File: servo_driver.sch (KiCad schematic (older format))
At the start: 16 parts

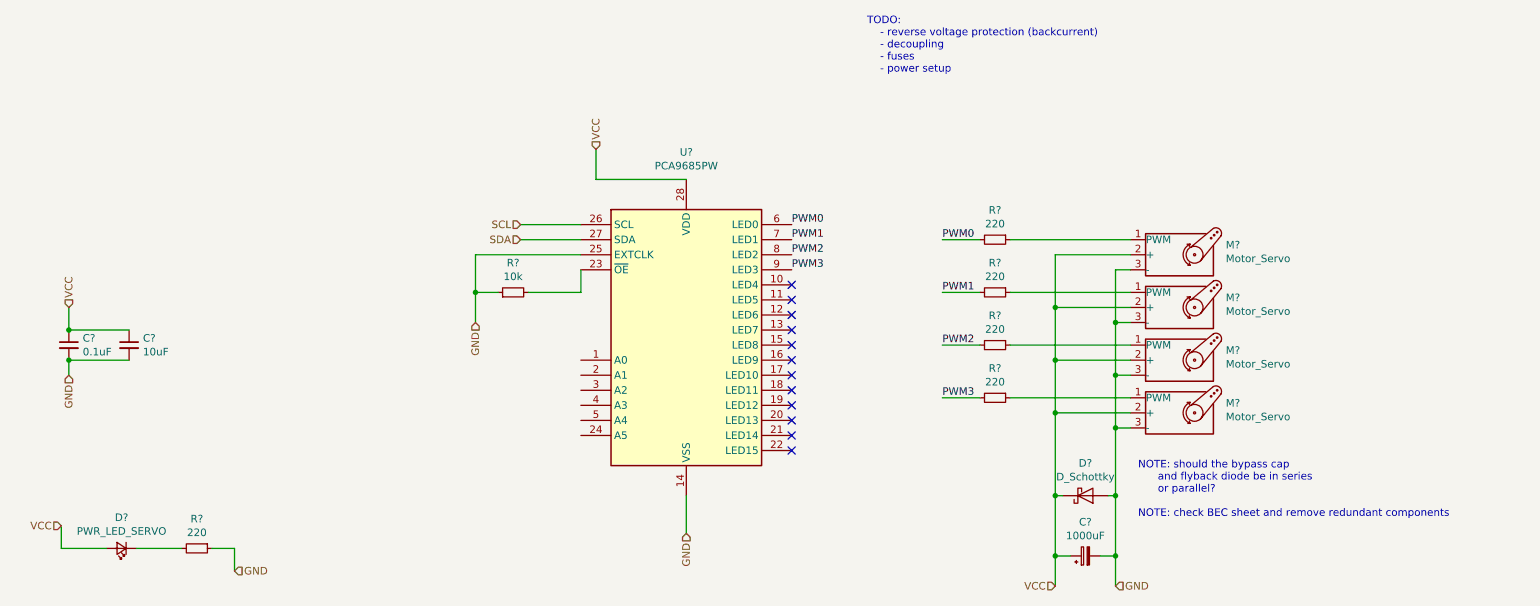
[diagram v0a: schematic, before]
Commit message: update reference ids, assign value to c8
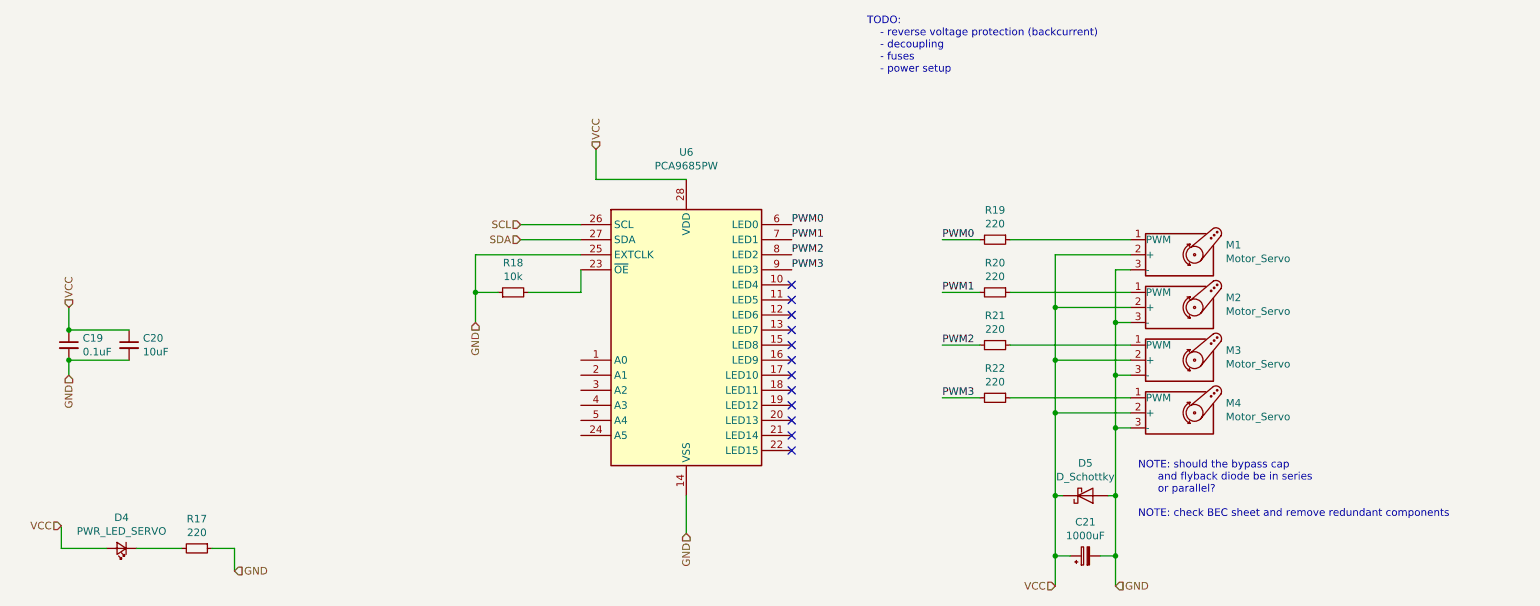
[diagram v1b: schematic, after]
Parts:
- gave numbers to parts that had none: 16
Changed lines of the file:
@@
 GND
 $Comp
-L Driver_LED:PCA9685PW U?
+L Driver_LED:PCA9685PW U6
 U 1 1 61AF04F5
 P 5800 3700
-F 0 "U?" H 5800 4881 50  0000 C CNN
+F 0 "U6" H 5800 4881 50  0000 C CNN
 F 1 "PCA9685PW" H 5800 4790 50  0000 C CNN
 F 2 "Package_SO:TSSOP-28_4.4x9.7mm_P0.65mm" H 5825 2725 50  0001 L CNN
@@
 $EndComp
 $Comp
-L Device:C_Small C?
+L Device:C_Small C20
 U 1 1 61AFE32D
 P 2100 3800
-F 0 "C?" H 2192 3846 50  0000 L CNN
+F 0 "C20" H 2192 3846 50  0000 L CNN
 F 1 "10uF" H 2192 3755 50  0000 L CNN
 F 2 "" H 2100 3800 50  0001 C CNN
@@
 $EndComp
 $Comp
-L Device:C_Small C?
+L Device:C_Small C19
 U 1 1 61AFE9E7
 P 1700 3800
-F 0 "C?" H 1792 3846 50  0000 L CNN
+F 0 "C19" H 1792 3846 50  0000 L CNN
 F 1 "0.1uF" H 1792 3755 50  0000 L CNN
 F 2 "" H 1700 3800 50  0001 C CNN
@@
 TODO:\n    - reverse voltage protection (backcurrent)\n    - decoupling\n    - fuses\n    - power setup\n
 $Comp
-L Device:R_Small R?
+L Device:R_Small R19
 U 1 1 61A44E55
 P 7850 3100
-F 0 "R?" V 7654 3100 50  0000 C CNN
+F 0 "R19" V 7654 3100 50  0000 C CNN
 F 1 "220" V 7745 3100 50  0000 C CNN
 F 2 "" H 7850 3100 50  0001 C CNN
@@
 $EndComp
 $Comp
-L Motor:Motor_Servo M?
+L Motor:Motor_Servo M1
 U 1 1 61AAC45D
 P 9050 3200
-F 0 "M?" H 9382 3265 50  0000 L CNN
+F 0 "M1" H 9382 3265 50  0000 L CNN
 F 1 "Motor_Servo" H 9382 3174 50  0000 L CNN
 F 2 "" H 9050 3010 50  0001 C CNN
@@
 $EndComp
 $Comp
-L Motor:Motor_Servo M?
+L Motor:Motor_Servo M2
 U 1 1 61AB6B78
 P 9050 3550
-F 0 "M?" H 9382 3615 50  0000 L CNN
+F 0 "M2" H 9382 3615 50  0000 L CNN
 F 1 "Motor_Servo" H 9382 3524 50  0000 L CNN
 F 2 "" H 9050 3360 50  0001 C CNN
@@
 $EndComp
 $Comp
-L Motor:Motor_Servo M?
+L Motor:Motor_Servo M3
 U 1 1 61AC1470
 P 9050 3900
-F 0 "M?" H 9382 3965 50  0000 L CNN
+F 0 "M3" H 9382 3965 50  0000 L CNN
 F 1 "Motor_Servo" H 9382 3874 50  0000 L CNN
 F 2 "" H 9050 3710 50  0001 C CNN
@@
 $EndComp
 $Comp
-L Motor:Motor_Servo M?
+L Motor:Motor_Servo M4
 U 1 1 61AC1476
 P 9050 4250
-F 0 "M?" H 9382 4315 50  0000 L CNN
+F 0 "M4" H 9382 4315 50  0000 L CNN
 F 1 "Motor_Servo" H 9382 4224 50  0000 L CNN
 F 2 "" H 9050 4060 50  0001 C CNN
@@
 PWM0
 $Comp
-L Device:R_Small R?
+L Device:R_Small R20
 U 1 1 61ACE5FC
 P 7850 3450
-F 0 "R?" V 7654 3450 50  0000 C CNN
+F 0 "R20" V 7654 3450 50  0000 C CNN
 F 1 "220" V 7745 3450 50  0000 C CNN
 F 2 "" H 7850 3450 50  0001 C CNN
@@
 PWM1
 $Comp
-L Device:R_Small R?
+L Device:R_Small R21
 U 1 1 61ACED83
 P 7850 3800
-F 0 "R?" V 7654 3800 50  0000 C CNN
+F 0 "R21" V 7654 3800 50  0000 C CNN
 F 1 "220" V 7745 3800 50  0000 C CNN
 F 2 "" H 7850 3800 50  0001 C CNN
@@
 PWM2
 $Comp
-L Device:R_Small R?
+L Device:R_Small R22
 U 1 1 61ACF554
 P 7850 4150
-F 0 "R?" V 7654 4150 50  0000 C CNN
+F 0 "R22" V 7654 4150 50  0000 C CNN
 F 1 "220" V 7745 4150 50  0000 C CNN
 F 2 "" H 7850 4150 50  0001 C CNN
@@
 	4400 3200 4400 3450
 $Comp
-L Device:R_Small R?
+L Device:R_Small R18
 U 1 1 61AEE150
 P 4650 3450
-F 0 "R?" V 4846 3450 50  0000 C CNN
+F 0 "R18" V 4846 3450 50  0000 C CNN
 F 1 "10k" V 4755 3450 50  0000 C CNN
 F 2 "" H 4650 3450 50  0001 C CNN
@@
 	4550 3450 4400 3450
 $Comp
-L Device:D_Schottky D?
+L Device:D_Schottky D5
 U 1 1 61B09031
 P 8450 4800
-F 0 "D?" H 8450 4584 50  0000 C CNN
+F 0 "D5" H 8450 4584 50  0000 C CNN
 F 1 "D_Schottky" H 8450 4675 50  0000 C CNN
 F 2 "" H 8450 4800 50  0001 C CNN
@@
 Connection ~ 8650 4800
 $Comp
-L Device:CP_Small C?
+L Device:CP_Small C21
 U 1 1 61B588AD
 P 8450 5200
-F 0 "C?" V 8675 5200 50  0000 C CNN
+F 0 "C21" V 8675 5200 50  0000 C CNN
 F 1 "1000uF" V 8584 5200 50  0000 C CNN
 F 2 "" H 8450 5200 50  0001 C CNN
@@
 NOTE: should the bypass cap \n      and flyback diode be in series\n      or parallel?\n\nNOTE: check BEC sheet and remove redundant components
 $Comp
-L Device:LED_Small D?
+L Device:LED_Small D4
 U 1 1 61B9D802
 P 2050 5150
-F 0 "D?" H 2050 4945 50  0000 C CNN
+F 0 "D4" H 2050 4945 50  0000 C CNN
 F 1 "PWR_LED_SERVO" H 2050 5036 50  0000 C CNN
 F 2 "" V 2050 5150 50  0001 C CNN
@@
 	2800 5150 2800 5300
 $Comp
-L Device:R_Small R?
+L Device:R_Small R17
 U 1 1 61BA0867
 P 2550 5150
-F 0 "R?" V 2354 5150 50  0000 C CNN
+F 0 "R17" V 2354 5150 50  0000 C CNN
 F 1 "220" V 2445 5150 50  0000 C CNN
 F 2 "" H 2550 5150 50  0001 C CNN

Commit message: no longer a hat lol
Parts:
- C19, C20: footprint (none) -> Capacitor_SMD:C_0805_2012Metric_Pad1.15x1.40mm_HandSolder
- CP21: renamed from C21; footprint (none) -> EEE-TP1J102M:CAP_EEETP1J102M
- D4: footprint (none) -> LED_SMD:LED_0805_2012Metric_Pad1.15x1.40mm_HandSolder
- D5: footprint (none) -> TO254P1521X483-4N:TO254P1521X483-4N
- M1, M2, M3, M4: footprint (none) -> Connector_PinHeader_2.54mm:PinHeader_1x03_P2.54mm_Vertical
- R17: value 220 -> 120; footprint (none) -> Resistor_SMD:R_0805_2012Metric_Pad1.15x1.40mm_HandSolder
- R18, R19, R20, R21, R22: footprint (none) -> Resistor_SMD:R_0805_2012Metric_Pad1.15x1.40mm_HandSolder
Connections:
- net VCC: no longer CP21.1, D5.1 (K), M1.2 (+), M2.2 (+), M3.2 (+), M4.2 (+)
- new net 5V_IN: CP21.1, D5.1 (K), M1.2 (+), M2.2 (+), M3.2 (+), M4.2 (+)
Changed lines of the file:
@@
 F 0 "C20" H 2192 3846 50  0000 L CNN
 F 1 "10uF" H 2192 3755 50  0000 L CNN
-F 2 "" H 2100 3800 50  0001 C CNN
+F 2 "Capacitor_SMD:C_0805_2012Metric_Pad1.15x1.40mm_HandSolder" H 2100 3800 50  0001 C CNN
 F 3 "~" H 2100 3800 50  0001 C CNN
 	1    2100 3800
@@
 F 0 "C19" H 1792 3846 50  0000 L CNN
 F 1 "0.1uF" H 1792 3755 50  0000 L CNN
-F 2 "" H 1700 3800 50  0001 C CNN
+F 2 "Capacitor_SMD:C_0805_2012Metric_Pad1.15x1.40mm_HandSolder" H 1700 3800 50  0001 C CNN
 F 3 "~" H 1700 3800 50  0001 C CNN
 	1    1700 3800
@@
 F 0 "R19" V 7654 3100 50  0000 C CNN
 F 1 "220" V 7745 3100 50  0000 C CNN
-F 2 "" H 7850 3100 50  0001 C CNN
+F 2 "Resistor_SMD:R_0805_2012Metric_Pad1.15x1.40mm_HandSolder" H 7850 3100 50  0001 C CNN
 F 3 "~" H 7850 3100 50  0001 C CNN
 	1    7850 3100
@@
 F 0 "M1" H 9382 3265 50  0000 L CNN
 F 1 "Motor_Servo" H 9382 3174 50  0000 L CNN
-F 2 "" H 9050 3010 50  0001 C CNN
+F 2 "Connector_PinHeader_2.54mm:PinHeader_1x03_P2.54mm_Vertical" H 9050 3010 50  0001 C CNN
 F 3 "http://forums.parallax.com/uploads/attachments/46831/74481.png" H 9050 3010 50  0001 C CNN
 	1    9050 3200
@@
 F 0 "M2" H 9382 3615 50  0000 L CNN
 F 1 "Motor_Servo" H 9382 3524 50  0000 L CNN
-F 2 "" H 9050 3360 50  0001 C CNN
+F 2 "Connector_PinHeader_2.54mm:PinHeader_1x03_P2.54mm_Vertical" H 9050 3360 50  0001 C CNN
 F 3 "http://forums.parallax.com/uploads/attachments/46831/74481.png" H 9050 3360 50  0001 C CNN
 	1    9050 3550
@@
 F 0 "M3" H 9382 3965 50  0000 L CNN
 F 1 "Motor_Servo" H 9382 3874 50  0000 L CNN
-F 2 "" H 9050 3710 50  0001 C CNN
+F 2 "Connector_PinHeader_2.54mm:PinHeader_1x03_P2.54mm_Vertical" H 9050 3710 50  0001 C CNN
 F 3 "http://forums.parallax.com/uploads/attachments/46831/74481.png" H 9050 3710 50  0001 C CNN
 	1    9050 3900
@@
 F 0 "M4" H 9382 4315 50  0000 L CNN
 F 1 "Motor_Servo" H 9382 4224 50  0000 L CNN
-F 2 "" H 9050 4060 50  0001 C CNN
+F 2 "Connector_PinHeader_2.54mm:PinHeader_1x03_P2.54mm_Vertical" H 9050 4060 50  0001 C CNN
 F 3 "http://forums.parallax.com/uploads/attachments/46831/74481.png" H 9050 4060 50  0001 C CNN
 	1    9050 4250
@@
 F 0 "R20" V 7654 3450 50  0000 C CNN
 F 1 "220" V 7745 3450 50  0000 C CNN
-F 2 "" H 7850 3450 50  0001 C CNN
+F 2 "Resistor_SMD:R_0805_2012Metric_Pad1.15x1.40mm_HandSolder" H 7850 3450 50  0001 C CNN
 F 3 "~" H 7850 3450 50  0001 C CNN
 	1    7850 3450
@@
 F 0 "R21" V 7654 3800 50  0000 C CNN
 F 1 "220" V 7745 3800 50  0000 C CNN
-F 2 "" H 7850 3800 50  0001 C CNN
+F 2 "Resistor_SMD:R_0805_2012Metric_Pad1.15x1.40mm_HandSolder" H 7850 3800 50  0001 C CNN
 F 3 "~" H 7850 3800 50  0001 C CNN
 	1    7850 3800
@@
 F 0 "R22" V 7654 4150 50  0000 C CNN
 F 1 "220" V 7745 4150 50  0000 C CNN
-F 2 "" H 7850 4150 50  0001 C CNN
+F 2 "Resistor_SMD:R_0805_2012Metric_Pad1.15x1.40mm_HandSolder" H 7850 4150 50  0001 C CNN
 F 3 "~" H 7850 4150 50  0001 C CNN
 	1    7850 4150
@@
 F 0 "R18" V 4846 3450 50  0000 C CNN
 F 1 "10k" V 4755 3450 50  0000 C CNN
-F 2 "" H 4650 3450 50  0001 C CNN
+F 2 "Resistor_SMD:R_0805_2012Metric_Pad1.15x1.40mm_HandSolder" H 4650 3450 50  0001 C CNN
 F 3 "~" H 4650 3450 50  0001 C CNN
 	1    4650 3450
@@
 F 0 "D5" H 8450 4584 50  0000 C CNN
 F 1 "D_Schottky" H 8450 4675 50  0000 C CNN
-F 2 "" H 8450 4800 50  0001 C CNN
+F 2 "TO254P1521X483-4N:TO254P1521X483-4N" H 8450 4800 50  0001 C CNN
 F 3 "~" H 8450 4800 50  0001 C CNN
 	1    8450 4800
@@
 Connection ~ 8650 4800
 $Comp
-L Device:CP_Small C21
+L Device:CP_Small CP21
 U 1 1 61B588AD
 P 8450 5200
-F 0 "C21" V 8675 5200 50  0000 C CNN
+F 0 "CP21" V 8675 5200 50  0000 C CNN
 F 1 "1000uF" V 8584 5200 50  0000 C CNN
-F 2 "" H 8450 5200 50  0001 C CNN
+F 2 "EEE-TP1J102M:CAP_EEETP1J102M" H 8450 5200 50  0001 C CNN
 F 3 "~" H 8450 5200 50  0001 C CNN
 	1    8450 5200
@@
 F 0 "D4" H 2050 4945 50  0000 C CNN
 F 1 "PWR_LED_SERVO" H 2050 5036 50  0000 C CNN
-F 2 "" V 2050 5150 50  0001 C CNN
+F 2 "LED_SMD:LED_0805_2012Metric_Pad1.15x1.40mm_HandSolder" V 2050 5150 50  0001 C CNN
 F 3 "~" V 2050 5150 50  0001 C CNN
 	1    2050 5150
@@
 P 2550 5150
 F 0 "R17" V 2354 5150 50  0000 C CNN
-F 1 "220" V 2445 5150 50  0000 C CNN
-F 2 "" H 2550 5150 50  0001 C CNN
+F 1 "120" V 2445 5150 50  0000 C CNN
+F 2 "Resistor_SMD:R_0805_2012Metric_Pad1.15x1.40mm_HandSolder" H 2550 5150 50  0001 C CNN
 F 3 "~" H 2550 5150 50  0001 C CNN
 	1    2550 5150
@@
 GND
 Text HLabel 8250 5400 0    50   Input ~ 0
-VCC
+5V_IN
 Text HLabel 8650 5400 2    50   Input ~ 0
 GND

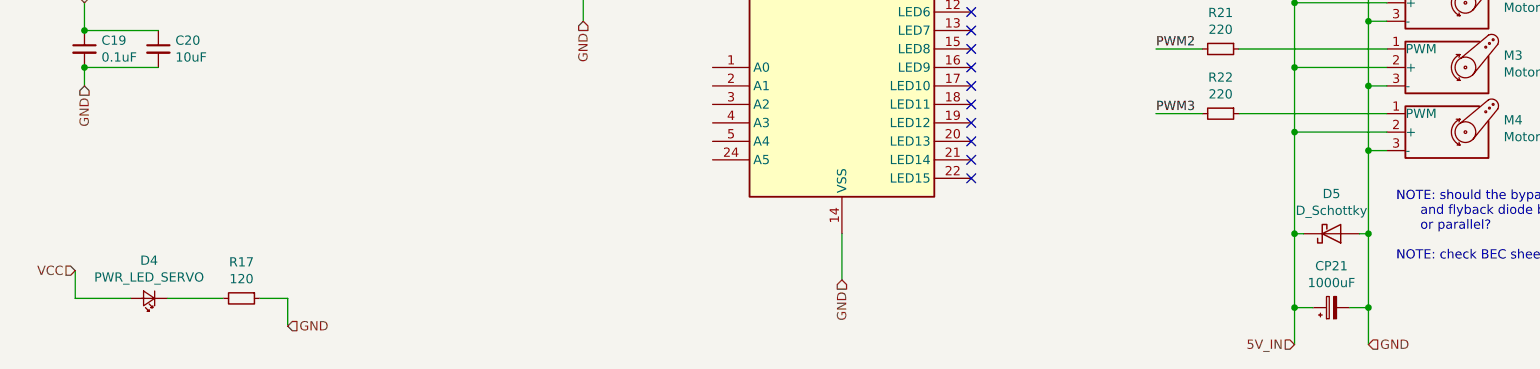
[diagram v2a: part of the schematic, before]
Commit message: [schematic] fix 3v3 symbol pin to use 3v3_pi instead of 5V_SRV
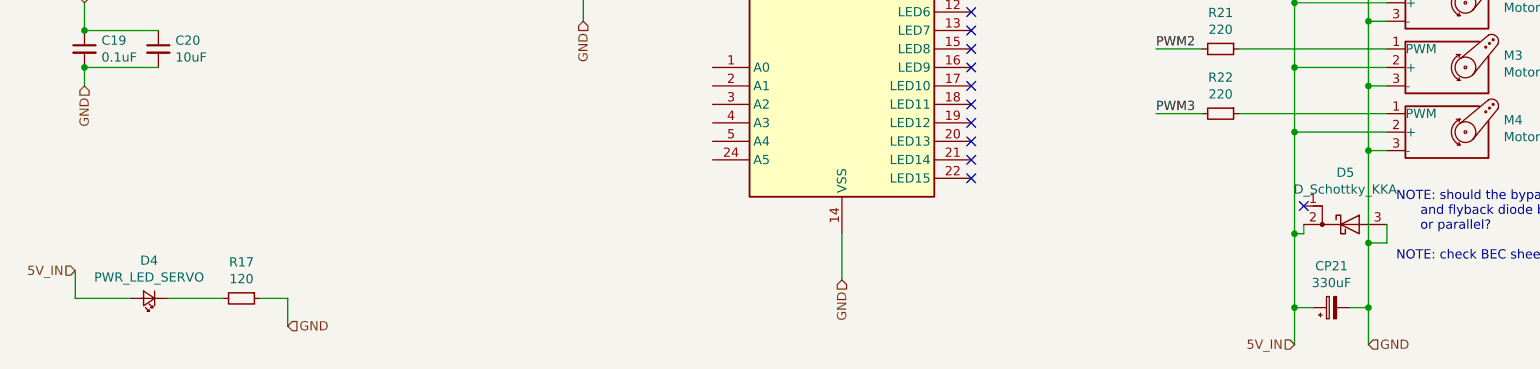
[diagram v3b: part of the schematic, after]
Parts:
- removed D5: D_Schottky, TO254P1521X483-4N:TO254P1521X483-4N, symbol Device:D_Schottky
- added D5: D_Schottky_KKA, TO254P1521X483-4N:TO254P1521X483-4N, symbol Device:D_Schottky_KKA
- CP21: value 1000uF -> 330uF; footprint EEE-TP1J102M:CAP_EEETP1J102M -> Capacitor_THT:CP_Radial_D10.0mm_P5.00mm
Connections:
- net 5V_IN: now also D4.2 (A), D5.2 (K)
- net GND: now also D5.3 (A)
- net VCC: no longer D4.2 (A)
- no-connect marks 12 -> 13
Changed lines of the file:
@@
 Wire Wire Line
 	4550 3450 4400 3450
-$Comp
-L Device:D_Schottky D5
-U 1 1 61B09031
-P 8450 4800
-F 0 "D5" H 8450 4584 50  0000 C CNN
-F 1 "D_Schottky" H 8450 4675 50  0000 C CNN
-F 2 "TO254P1521X483-4N:TO254P1521X483-4N" H 8450 4800 50  0001 C CNN
-F 3 "~" H 8450 4800 50  0001 C CNN
-	1    8450 4800
-	1    0    0    1
-$EndComp
 Connection ~ 8250 3550
 Wire Wire Line
@@
 	8300 4800 8250 4800
 Connection ~ 8250 4800
-Wire Wire Line
-	8650 4350 8650 4800
-Wire Wire Line
-	8650 4800 8600 4800
-Connection ~ 8650 4800
 $Comp
 L Device:CP_Small CP21
@@
 P 8450 5200
 F 0 "CP21" V 8675 5200 50  0000 C CNN
-F 1 "1000uF" V 8584 5200 50  0000 C CNN
-F 2 "EEE-TP1J102M:CAP_EEETP1J102M" H 8450 5200 50  0001 C CNN
+F 1 "330uF" V 8584 5200 50  0000 C CNN
+F 2 "Capacitor_THT:CP_Radial_D10.0mm_P5.00mm" H 8450 5200 50  0001 C CNN
 F 3 "~" H 8450 5200 50  0001 C CNN
 	1    8450 5200
@@
 Wire Wire Line
 	8650 5200 8550 5200
-Wire Wire Line
-	8650 4800 8650 5200
 Wire Wire Line
 	8250 5200 8350 5200
@@
 	2150 5150 2450 5150
 Text HLabel 1650 5000 0    50   Input ~ 0
-VCC
+5V_IN
 Text HLabel 2800 5300 2    50   Input ~ 0
 GND
@@
 NoConn ~ 6500 4400
 NoConn ~ 6500 4500
+$Comp
+L Device:D_Schottky_KKA D5
+U 1 1 61ACD2D1
+P 8550 4750
+F 0 "D5" H 8525 5031 50  0000 C CNN
+F 1 "D_Schottky_KKA" H 8525 4940 50  0000 C CNN
+F 2 "TO254P1521X483-4N:TO254P1521X483-4N" H 8550 4750 50  0001 C CNN
+F 3 "~" H 8550 4750 50  0001 C CNN
+	1    8550 4750
+	1    0    0    -1
+$EndComp
+Wire Wire Line
+	8650 4350 8650 4850
+Wire Wire Line
+	8300 4750 8300 4800
+NoConn ~ 8300 4650
+Wire Wire Line
+	8750 4750 8750 4850
+Wire Wire Line
+	8750 4850 8650 4850
+Connection ~ 8650 4850
+Wire Wire Line
+	8650 4850 8650 5200
 $EndSCHEMATC

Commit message: power supply overhaul
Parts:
- C15: renamed from C19; footprint Capacitor_SMD:C_0805_2012Metric_Pad1.15x1.40mm_HandSolder -> Capacitor_SMD:C_0603_1608Metric_Pad1.05x0.95mm_HandSolder; Description (none) -> 16V MLCC 10%; Manufacturer_Part_Number (none) -> C0603C104K4RACTU; category (none) -> SERVO; package (none) -> 0603
- C16: renamed from C20; footprint Capacitor_SMD:C_0805_2012Metric_Pad1.15x1.40mm_HandSolder -> Capacitor_SMD:C_0603_1608Metric_Pad1.05x0.95mm_HandSolder; Description (none) -> 25V MLCC 10%; Manufacturer_Part_Number (none) -> GRM188R61E106KA73J; category (none) -> SERVO; package (none) -> 0603
- CP2: renamed from CP21; Description (none) -> 100V Electrolytic 20%; Manufacturer_Part_Number (none) -> 337CKS050M; category (none) -> SERVO; package (none) -> 16mm
- D5: renamed from D4; Description (none) -> 2.1V Amber LED 20mA; Manufacturer_Part_Number (none) -> HSMA-C170; category (none) -> SERVO; package (none) -> 0805
- D6: renamed from D5; footprint TO254P1521X483-4N:TO254P1521X483-4N -> Diode_SMD:D_SOD-128; Description (none) -> Schottky Diode; Manufacturer_Part_Number (none) -> RB088LAM-40TR; category (none) -> SERVO; package (none) -> SOD-128-2
- M1, M2, M3, M4: Description (none) -> 1x3 2.45mm Pitch Pin Header (Male); category (none) -> SERVO; package (none) -> 3x1x2.54mm
- R18: renamed from R17; value 120 -> 150; Description (none) -> 125mW Resistor 0.1%; Manufacturer_Part_Number (none) -> RP73D2A150RBTG; category (none) -> SERVO; package (none) -> 0805
- R19: renamed from R18; Description (none) -> 0.2W Resistor 0.1%; Manufacturer_Part_Number (none) -> PTN0805Y1002BST1; category (none) -> SERVO; package (none) -> 0805
- R20: renamed from R19; footprint Resistor_SMD:R_0805_2012Metric_Pad1.15x1.40mm_HandSolder -> Resistor_SMD:R_1206_3216Metric_Pad1.42x1.75mm_HandSolder; Description (none) -> 1W Resistor 0.1%; Manufacturer_Part_Number (none) -> HRG3216P-2200-B-T1; category (none) -> SERVO; package (none) -> 1206
- R21: renamed from R20; footprint Resistor_SMD:R_0805_2012Metric_Pad1.15x1.40mm_HandSolder -> Resistor_SMD:R_1206_3216Metric_Pad1.42x1.75mm_HandSolder; Description (none) -> 1W Resistor 0.1%; Manufacturer_Part_Number (none) -> HRG3216P-2200-B-T1; category (none) -> SERVO; package (none) -> 1206
- R22: renamed from R21; footprint Resistor_SMD:R_0805_2012Metric_Pad1.15x1.40mm_HandSolder -> Resistor_SMD:R_1206_3216Metric_Pad1.42x1.75mm_HandSolder; Description (none) -> 1W Resistor 0.1%; Manufacturer_Part_Number (none) -> HRG3216P-2200-B-T1; category (none) -> SERVO; package (none) -> 1206
- R23: renamed from R22; footprint Resistor_SMD:R_0805_2012Metric_Pad1.15x1.40mm_HandSolder -> Resistor_SMD:R_1206_3216Metric_Pad1.42x1.75mm_HandSolder; Description (none) -> 1W Resistor 0.1%; Manufacturer_Part_Number (none) -> HRG3216P-2200-B-T1; category (none) -> SERVO; package (none) -> 1206
- U5: renamed from U6; Description (none) -> PCA9685 i2c LED Driver; Manufacturer_Part_Number (none) -> PCA9685PW; category (none) -> SERVO; package (none) -> TSSOP-28
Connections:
- no-connect marks 13 -> 19

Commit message: final final sch
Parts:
- CP2: value 330uF -> 470uF; footprint Capacitor_THT:CP_Radial_D10.0mm_P5.00mm -> Capacitor_SMD:CP_Elec_10x10.5; Description 100V Electrolytic 20% -> 6.3V SMD Electrolytic 20%; Manufacturer_Part_Number 337CKS050M -> APXH6R3ARA471MJ80G; category SERVO -> 5VREG; package 16mm -> (none)
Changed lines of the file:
@@
 	8300 4800 8250 4800
 Connection ~ 8250 4800
-$Comp
-L Device:CP_Small CP2
-U 1 1 61B588AD
-P 8450 5200
-F 0 "CP2" V 8675 5200 50  0000 C CNN
-F 1 "330uF" V 8584 5200 50  0000 C CNN
-F 2 "Capacitor_THT:CP_Radial_D10.0mm_P5.00mm" H 8450 5200 50  0001 C CNN
-F 3 "~" H 8450 5200 50  0001 C CNN
-F 4 "100V Electrolytic 20%" H 8450 5200 50  0001 C CNN "Description"
-F 5 "337CKS050M" H 8450 5200 50  0001 C CNN "Manufacturer_Part_Number"
-F 6 "SERVO" H 8450 5200 50  0001 C CNN "category"
-F 7 "16mm" H 8450 5200 50  0001 C CNN "package"
-	1    8450 5200
-	0    -1   -1   0
-$EndComp
 Wire Wire Line
 	8250 4800 8250 5200
@@
 NoConn ~ 5100 4300
 NoConn ~ 5100 4400
+$Comp
+L Device:CP_Small CP?
+U 1 1 61B9AE87
+P 8450 5200
+AR Path="/61BC5F5B/61B9AE87" Ref="CP?"  Part="1"
+AR Path="/61AC98FF/61B9AE87" Ref="CP2"  Part="1"
+F 0 "CP2" H 8538 5246 50  0000 L CNN
+F 1 "470uF" H 8538 5155 50  0000 L CNN
+F 2 "Capacitor_SMD:CP_Elec_10x10.5" H 8450 5200 50  0001 C CNN
+F 3 "~" H 8450 5200 50  0001 C CNN
+F 4 "6.3V SMD Electrolytic 20%" H 8450 5200 50  0001 C CNN "Description"
+F 5 "APXH6R3ARA471MJ80G" H 8450 5200 50  0001 C CNN "Manufacturer_Part_Number"
+F 6 "5VREG" H 8450 5200 50  0001 C CNN "category"
+	1    8450 5200
+	0    -1   -1   0
+$EndComp
 $EndSCHEMATC
